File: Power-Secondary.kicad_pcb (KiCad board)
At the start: 4 copper layers, 79.4 x 58.3 mm, 102 parts, among them J3 PowerConn, J5 Conn_01x03, Q1 SQJQ140E-T1_GE3, Q2 SQJQ140E-T1_GE3, Q3 SQJQ140E-T1_GE3, Q4 SQJQ140E-T1_GE3, Q5 SQJ141ELP, Q6 NMOS, Q7 PMOS, U1 LM397, U2 LTC4421CG-PBF, U3 74LVC2G07GV,125, U4 74LVC2G07GV,125, U5 74LVC2G07GV,125

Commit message: bruh changes
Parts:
- removed DCDC_FAULT, SUPP_FAULT: LED, LED_SMD:LED_0805_2012Metric
- removed the G*** at (112.8, 65.8)
- removed R11, R12, R17: 100K, Resistor_SMD:R_0805_2012Metric
- removed U3: 74LVC2G07GV,125, Package_TO_SOT_SMD:ROHM_SOT-457_ClockwisePinNumbering
- Q6: footprint Package_TO_SOT_SMD:SOT-23 -> Package_TO_SOT_SMD:TSOT-23
- U1: footprint Package_TO_SOT_SMD:SOT-23-5 -> Package_TO_SOT_SMD:SOT-353_SC-70-5
- U4, U5: footprint Package_TO_SOT_SMD:ROHM_SOT-457_ClockwisePinNumbering -> Package_TO_SOT_SMD:SC-74-6_1.55x2.9mm_P0.95mm
- moved U1 0.63 mm to (143.6, 74.0)
- moved Q6 0.52 mm to (147.7, 98.2)
- moved INTVCC 0.22 mm to (129.6, 100.2)
- moved R18 0.20 mm to (141.0, 72.2)
- turned U4 to 90 degrees
- turned U5 to 90 degrees
- renumbered TP1 to INTVCC
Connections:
- R14 pad 2: Net-(U4-2Y) -> Net-(U4-1Y)
- R16 pad 2: Net-(U5-2Y) -> Net-(U5-1Y)
- U4 pad 1: /LTC4421/VALID2 -> /LTC4421/CH2
- U4 pad 3: /LTC4421/CH2 -> /LTC4421/VALID2
- U4 pad 4: Net-(U4-2Y) -> /SHDN_sig
- U4 pad 6: /SHDN_sig -> Net-(U4-1Y)
- U5 pad 1: /LTC4421/CH1 -> /LTC4421/VALID1
- U5 pad 3: /LTC4421/VALID1 -> /LTC4421/CH1
- U5 pad 4: Net-(U5-2Y) -> /LTC4421/Non-Crit Drive
- U5 pad 6: /LTC4421/Non-Crit Drive -> Net-(U5-1Y)
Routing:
- net /V2: track 74.0 -> 15.8 mm, vias 23 -> 17
- net Net-(U3-1Y): track 27.6 -> 0.00 mm, vias 1 -> 0
- net Net-(U3-2Y): track 27.5 -> 0.00 mm, vias 1 -> 0
- net Net-(U5-2Y): track 22.9 -> 0.00 mm, vias 2 -> 0
- net Net-(U5-1Y): track 0.00 -> 22.9 mm, vias 0 -> 2
- net Net-(U4-2Y): track 19.1 -> 0.00 mm, vias 2 -> 0
- net Net-(U4-1Y): track 0.00 -> 19.1 mm, vias 0 -> 2
- net /LTC4421/INTVCC: track 67.8 -> 56.5 mm
- net /LTC4421/FAULT2: track 21.6 -> 14.1 mm
- net /LTC4421/FAULT1: track 20.0 -> 16.1 mm, vias 3 -> 1
- net /SHDN_sig: track 37.8 -> 41.1 mm
- net Net-(Q5-Pad4): track 10.5 -> 7.77 mm
- net GND: track 12.3 -> 10.4 mm, vias 14 -> 13
- net /LTC4421/CH2: track 25.7 -> 27.6 mm
- net /LTC4421/VALID2: track 22.0 -> 23.6 mm
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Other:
- board text added: "EN"

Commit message: more bruh changes
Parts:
- U1: value LM397 -> TLV9061QDCKRQ1
- moved U1 0.32 mm to (143.7, 74.3), turned to 0 degrees
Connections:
- U1 pad 1: /LTC4421/INTVCC -> /LTC4421/Non-Crit Drive
- U1 pad 3: /LTC4421/Non-Crit Drive -> /LTC4421/INTVCC
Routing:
- net Net-(Q5-Pad4): track 7.77 -> 9.32 mm
- net /LTC4421/INTVCC: track 56.5 -> 57.1 mm
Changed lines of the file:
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@@
 	(footprint "Package_TO_SOT_SMD:SOT-353_SC-70-5"
 		(layer "B.Cu")
-		(at 143.6 74 90)
+		(at 143.7 74.3)
 		(descr "SOT-353, SC-70-5")
 		(tags "SOT-353 SC-70-5")
 		(property "Reference" "U1"
-			(at 0 2.25 90)
+			(at 0 2.25 0)
 			(layer "B.SilkS")
 			(effects
@@
 			)
 		)
-		(property "Value" "LM397"
-			(at 0 -2 90)
+		(property "Value" "TLV9061QDCKRQ1"
+			(at 0 -2 0)
 			(layer "B.Fab")
 			(effects
@@
 		)
 		(property "Datasheet" "http://www.ti.com/lit/ds/symlink/lm397.pdf"
-			(at 0 0 270)
+			(at 0 0 180)
 			(unlocked yes)
 			(layer "B.Fab")
@@
 		)
 		(property "Description" "Single General-Purpose Voltage Comparator with Open-Collector Output, SOT-23-5"
-			(at 0 0 270)
+			(at 0 0 180)
 			(unlocked yes)
 			(layer "B.Fab")
@@
 		(attr smd)
 		(fp_line
-			(start -0.7 -1.16)
-			(end 0.7 -1.16)
+			(start -0.71 1.16)
+			(end 0.7 1.16)
 			(stroke
 				(width 0.12)
@@
 		)
 		(fp_line
-			(start -0.71 1.16)
-			(end 0.7 1.16)
+			(start -0.7 -1.16)
+			(end 0.7 -1.16)
 			(stroke
 				(width 0.12)
@@
 		)
 		(fp_line
-			(start 1.6 -1.4)
-			(end 1.6 1.4)
+			(start -1.6 -1.4)
+			(end 1.6 -1.4)
 			(stroke
 				(width 0.05)
@@
 		)
 		(fp_line
-			(start -1.6 -1.4)
-			(end 1.6 -1.4)
+			(start -1.6 1.4)
+			(end -1.6 -1.4)
 			(stroke
 				(width 0.05)
@@
 		(fp_line
 			(start -1.6 1.4)
-			(end -1.6 -1.4)
+			(end 1.6 1.4)
 			(stroke
 				(width 0.05)
@@
 		)
 		(fp_line
-			(start -1.6 1.4)
+			(start 1.6 -1.4)
 			(end 1.6 1.4)
 			(stroke
@@
 		)
 		(fp_line
-			(start 0.675 -1.1)
+			(start -0.675 0.6)
 			(end -0.675 -1.1)
 			(stroke
@@
 		)
 		(fp_line
-			(start -0.675 0.6)
-			(end -0.675 -1.1)
+			(start -0.175 1.1)
+			(end -0.675 0.6)
 			(stroke
 				(width 0.1)
@@
 		)
 		(fp_line
-			(start 0.675 1.1)
-			(end 0.675 -1.1)
+			(start 0.675 -1.1)
+			(end -0.675 -1.1)
 			(stroke
 				(width 0.1)
@@
 		)
 		(fp_line
-			(start -0.175 1.1)
-			(end -0.675 0.6)
+			(start 0.675 1.1)
+			(end 0.675 -1.1)
 			(stroke
 				(width 0.1)
@@
 		)
 		(fp_text user "${REFERENCE}"
-			(at 0 0 0)
+			(at 0 0 90)
 			(layer "B.Fab")
 			(effects
@@
 		)
 		(pad "1" smd roundrect
-			(at -0.95 0.65 90)
+			(at -0.95 0.65)
 			(size 0.65 0.4)
 			(layers "B.Cu" "B.Mask" "B.Paste")
 			(roundrect_rratio 0.25)
-			(net 44 "/LTC4421/INTVCC")
-			(pinfunction "-")
+			(net 25 "/LTC4421/Non-Crit Drive")
+			(pinfunction "+")
 			(pintype "input")
 		)
 		(pad "2" smd roundrect
-			(at -0.95 0 90)
+			(at -0.95 0)
 			(size 0.65 0.4)
 			(layers "B.Cu" "B.Mask" "B.Paste")
@@
 		)
 		(pad "3" smd roundrect
-			(at -0.95 -0.65 90)
+			(at -0.95 -0.65)
 			(size 0.65 0.4)
 			(layers "B.Cu" "B.Mask" "B.Paste")
 			(roundrect_rratio 0.25)
-			(net 25 "/LTC4421/Non-Crit Drive")
-			(pinfunction "+")
+			(net 44 "/LTC4421/INTVCC")
+			(pinfunction "-")
 			(pintype "input")
 		)
 		(pad "4" smd roundrect
-			(at 0.95 -0.65 90)
+			(at 0.95 -0.65)
 			(size 0.65 0.4)
 			(layers "B.Cu" "B.Mask" "B.Paste")
@@
 		)
 		(pad "5" smd roundrect
-			(at 0.95 0.65 90)
+			(at 0.95 0.65)
 			(size 0.65 0.4)
 			(layers "B.Cu" "B.Mask" "B.Paste")
@@
 	)
 	(segment
-		(start 139.075 73.275)
-		(end 114.8 73.275)
+		(start 140.325 74.8)
+		(end 140.325 74.525)
 		(width 0.25)
 		(layer "F.Cu")
@@
 	)
 	(segment
-		(start 140.75 74.95)
+		(start 140.325 74.525)
 		(end 139.075 73.275)
 		(width 0.25)
@@
 		(net 25)
 	)
+	(segment
+		(start 139.075 73.275)
+		(end 114.8 73.275)
+		(width 0.25)
+		(layer "F.Cu")
+		(net 25)
+	)
 	(via
-		(at 140.75 74.95)
+		(at 140.325 74.8)
 		(size 0.8)
 		(drill 0.4)
@@
 	)
 	(segment
-		(start 140.75 74.95)
-		(end 142.95 74.95)
+		(start 140.325 74.8)
+		(end 140.475 74.95)
 		(width 0.25)
 		(layer "B.Cu")
@@
 	)
 	(segment
+		(start 140.475 74.95)
+		(end 142.75 74.95)
+		(width 0.25)
+		(layer "B.Cu")
+		(net 25)
+	)
+	(segment
 		(start 124.25 85.45)
 		(end 121.1 82.3)
@@
 	)
 	(segment
-		(start 145.15 75.85)
-		(end 144.25 74.95)
+		(start 145.15 75.45)
+		(end 144.65 74.95)
 		(width 0.25)
 		(layer "B.Cu")
@@
 	)
 	(segment
-		(start 145.15 81.75)
-		(end 145.15 75.85)
+		(start 143.65 73.65)
+		(end 142.75 73.65)
 		(width 0.25)
 		(layer "B.Cu")
@@
 	)
 	(segment
-		(start 144.25 74.95)
-		(end 144.25 73.05)
+		(start 144.65 74.65)
+		(end 143.65 73.65)
+		(width 0.25)
+		(layer "B.Cu")
+		(net 44)
+	)
+	(segment
+		(start 144.65 74.95)
+		(end 144.65 74.65)
+		(width 0.25)
+		(layer "B.Cu")
+		(net 44)
+	)
+	(segment
+		(start 145.15 81.75)
+		(end 145.15 75.45)
 		(width 0.25)
 		(layer "B.Cu")
@@
 	)
 	(segment
-		(start 144.687347 72.125)
-		(end 143.875 72.125)
+		(start 144.7 72.137653)
+		(end 144.687347 72.125)
 		(width 0.25)
 		(layer "B.Cu")
@@
 	)
 	(segment
-		(start 143.875 72.125)
-		(end 142.95 73.05)
+		(start 144.65 73.65)
+		(end 144.7 73.6)
 		(width 0.25)
 		(layer "B.Cu")
@@
 	)
 	(segment
-		(start 142.8875 73.1125)
-		(end 142.95 73.05)
+		(start 143.712347 73.1)
+		(end 141.0125 73.1)
 		(width 0.25)
 		(layer "B.Cu")
@@
 	)
 	(segment
-		(start 141 73.1125)
-		(end 142.8875 73.1125)
+		(start 141.0125 73.1)
+		(end 141 73.1125)
+		(width 0.25)
+		(layer "B.Cu")
+		(net 47)
+	)
+	(segment
+		(start 144.7 73.6)
+		(end 144.7 72.137653)
+		(width 0.25)
+		(layer "B.Cu")
+		(net 47)
+	)
+	(segment
+		(start 144.687347 72.125)
+		(end 143.712347 73.1)
 		(width 0.25)
 		(layer "B.Cu")

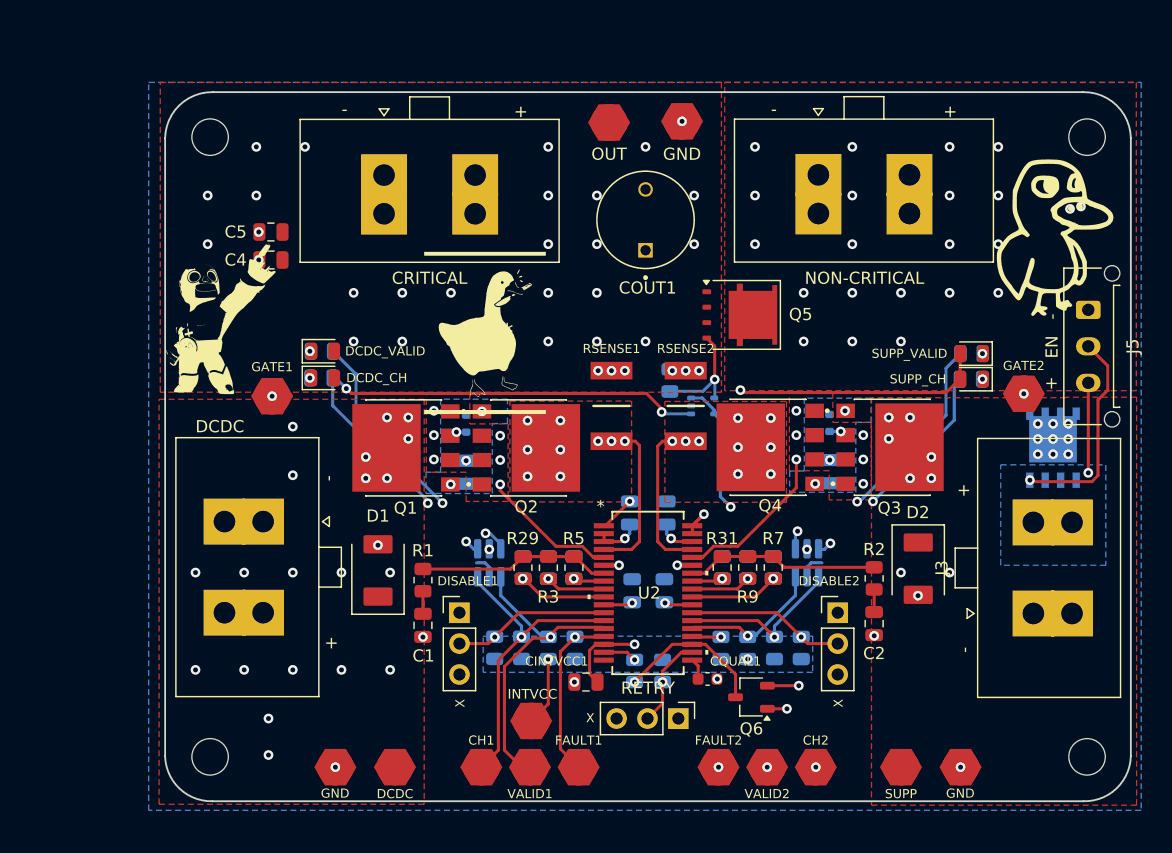
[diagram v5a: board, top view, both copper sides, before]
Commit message: Non-crit layout
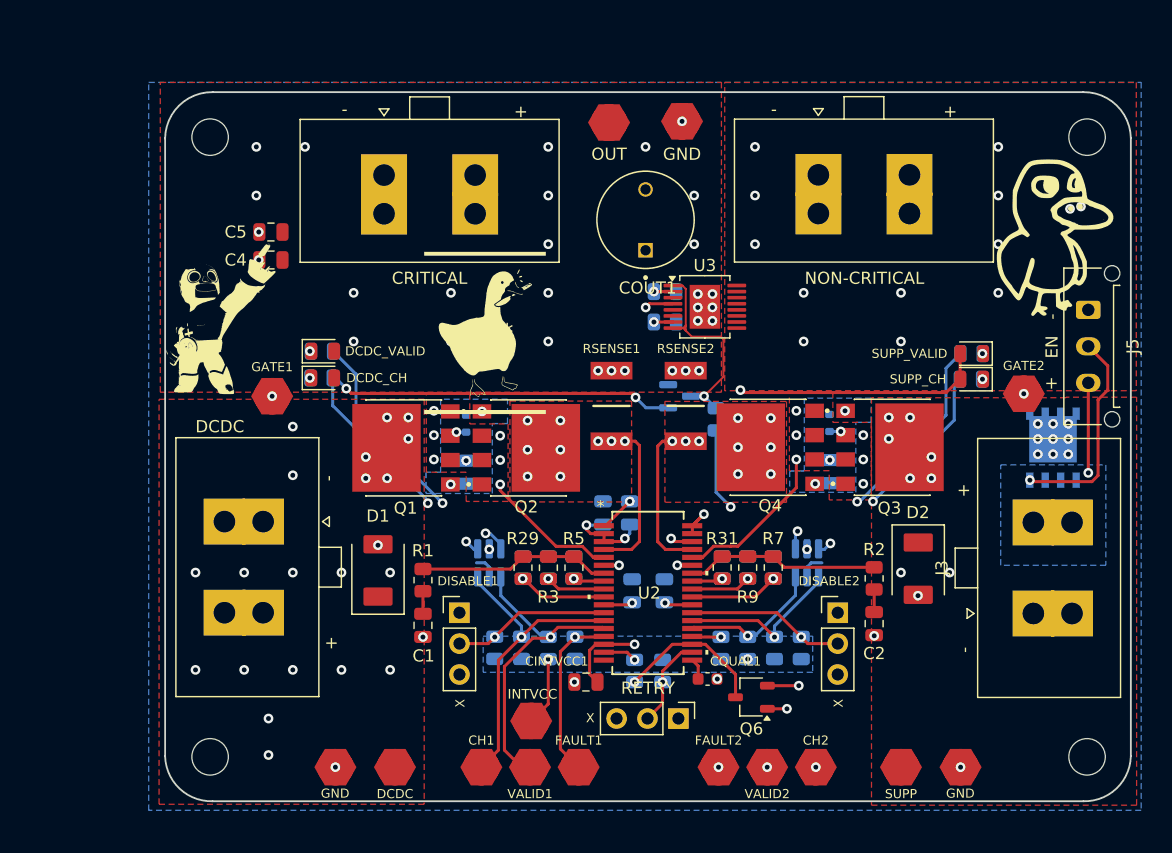
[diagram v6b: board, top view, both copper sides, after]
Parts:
- removed Q5: SQJ141ELP, Package_SO:PowerPAK_SO-8L_Single
- removed R18: 10K, Resistor_SMD:R_0805_2012Metric
- removed U1: TLV9061QDCKRQ1, Package_TO_SOT_SMD:SOT-353_SC-70-5
- added Q8: 2N7002, Package_TO_SOT_SMD:SOT-23, B.Cu at (141.8, 73.5)
- added R11: 100k, Resistor_SMD:R_0805_2012Metric, B.Cu at (144.8, 75.4)
- added R12: 1k, Resistor_SMD:R_0805_2012Metric, B.Cu at (140.6, 67.4)
- added R17: 15k, Resistor_SMD:R_0805_2012Metric, B.Cu at (140.6, 64.9)
- added U3: VND9016AJ, Package_SO:PowerSSO-16-1EP_3.9x4.9mm_P0.5mm_EP2.5x3.61mm, F.Cu at (143.9, 66.2)
- moved C3 5.25 mm to (135.5, 83.1)
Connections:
- net /LTC4421/Non-Crit Drive renamed /Non-Crit Drive
- CINTVCC1 pad 1: /LTC4421/INTVCC -> /INTVCC
- R19 pad 1: /LTC4421/INTVCC -> /INTVCC
- R20 pad 1: /LTC4421/INTVCC -> /INTVCC
- R21 pad 1: /LTC4421/INTVCC -> /INTVCC
- R22 pad 1: /LTC4421/INTVCC -> /INTVCC
- R23 pad 1: /LTC4421/INTVCC -> /INTVCC
- R24 pad 1: /LTC4421/INTVCC -> /INTVCC
- R25 pad 1: /LTC4421/INTVCC -> /INTVCC
- R26 pad 1: /LTC4421/INTVCC -> /INTVCC
- R27 pad 1: /LTC4421/INTVCC -> /INTVCC
- R28 pad 1: /LTC4421/INTVCC -> /INTVCC
- U2 pad 16: /LTC4421/INTVCC -> /INTVCC
- U2 pad 17: /LTC4421/INTVCC -> /INTVCC
- U4 pad 5: /LTC4421/INTVCC -> /INTVCC
- U5 pad 5: /LTC4421/INTVCC -> /INTVCC
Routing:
- net /LTC4421/INTVCC: track 57.1 -> 16.7 mm, vias 7 -> 2
- net /INTVCC: track 0.00 -> 36.3 mm, vias 0 -> 5
- net Net-(Q8-D): track 0.00 -> 17.2 mm, vias 0 -> 1
- net Net-(Q5-Pad4): track 9.32 -> 0.00 mm, vias 1 -> 0
- net GND: track 10.4 -> 12.7 mm, vias 13 -> 14
- net /Non-Crit Drive: track 50.1 -> 47.8 mm
- net /OUT: track 63.1 -> 65.1 mm, vias 35 -> 31
- net Net-(U3-~{FAULTRST}): track 0.00 -> 1.56 mm, vias 0 -> 1
- net Net-(U3-CS): track 0.00 -> 1.56 mm, vias 0 -> 1
- net Net-(J4-Pin_2): vias 22 -> 13
- added copper zone on B.Cu, net /INTVCC
- removed copper zone on B.Cu, net /LTC4421/INTVCC

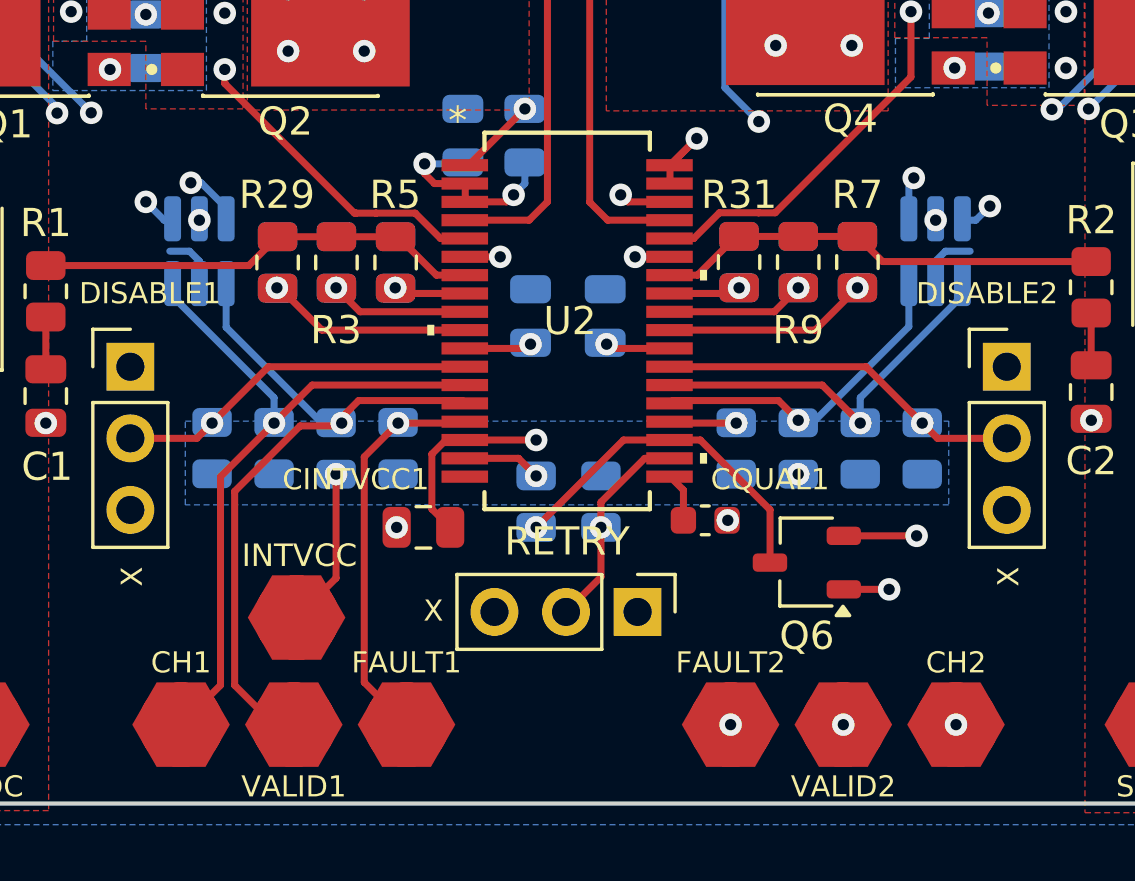
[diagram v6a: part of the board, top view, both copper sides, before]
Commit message: addressing DRC errors
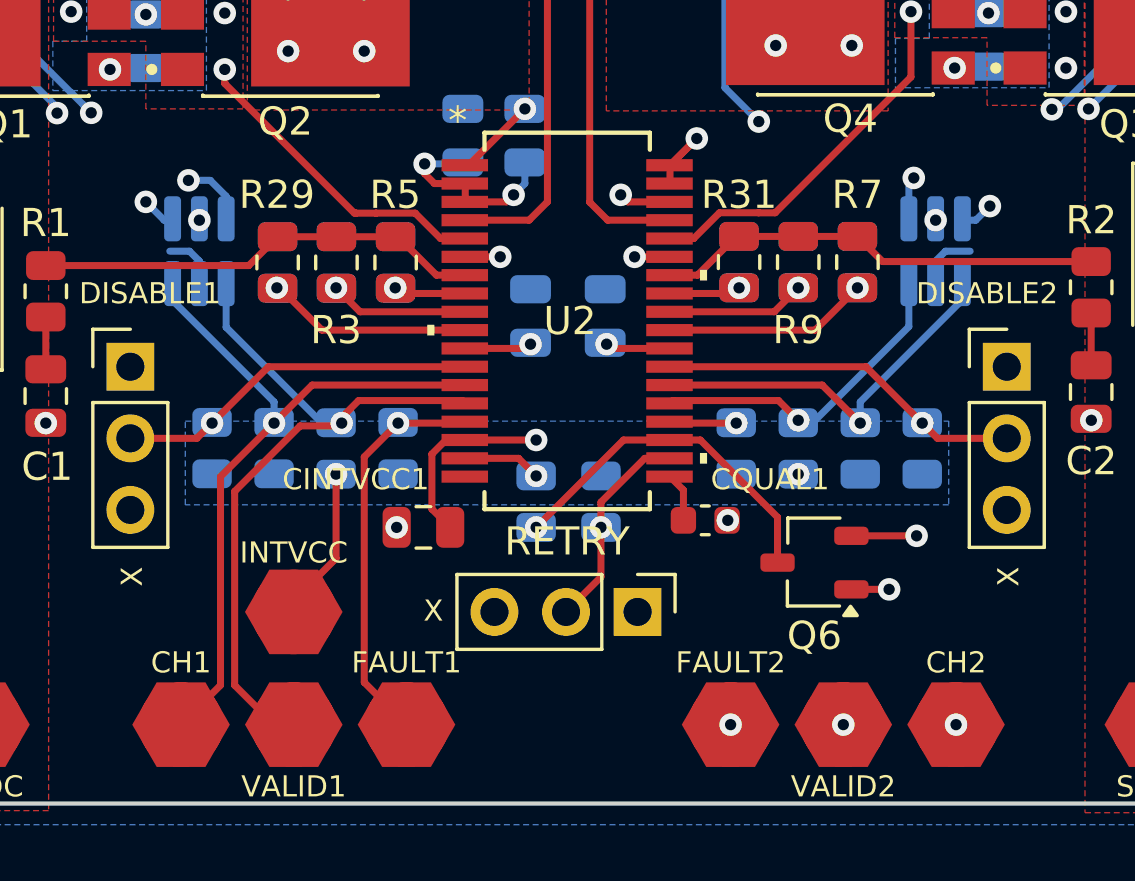
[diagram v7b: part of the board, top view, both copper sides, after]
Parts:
- moved Q6 0.27 mm to (148.0, 98.2)
- moved INTVCC 0.22 mm to (129.5, 100.0)
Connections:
- INTVCC pad 1: /LTC4421/INTVCC -> /INTVCC
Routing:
- net /LTC4421/INTVCC: track 16.7 -> 0.00 mm, vias 2 -> 0
- net /INTVCC: track 36.3 -> 52.5 mm, vias 5 -> 7
- net /LTC4421/FAULT1: track 16.1 -> 14.2 mm
- net /LTC4421/CH2: track 27.6 -> 26.6 mm
- net Net-(U5-1Y): track 22.9 -> 23.5 mm
- net GND: track 12.7 -> 12.1 mm

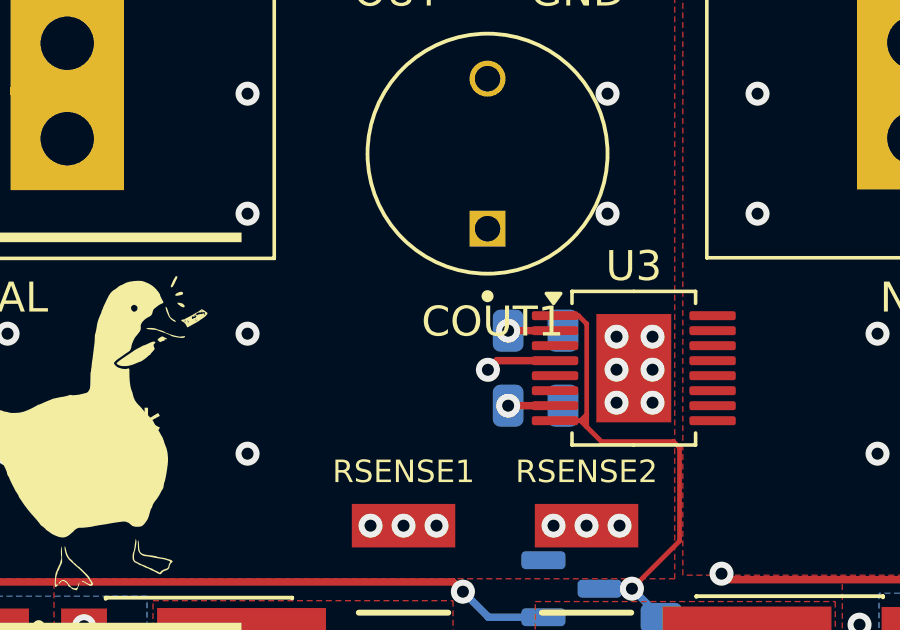
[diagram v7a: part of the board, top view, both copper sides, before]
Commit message: removed changxu's face
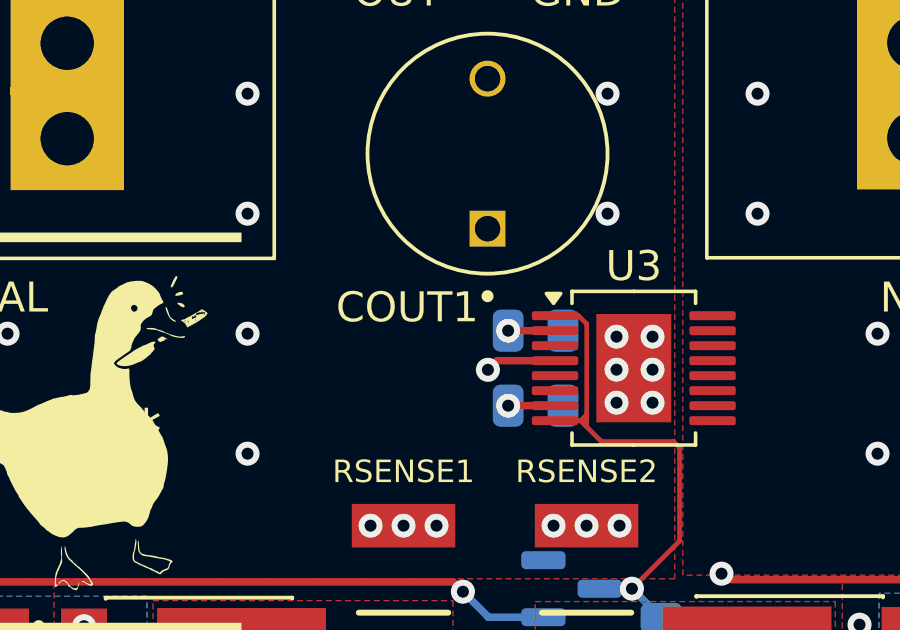
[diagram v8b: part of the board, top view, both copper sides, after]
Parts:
- removed the G*** at (139.1, 62.9)
